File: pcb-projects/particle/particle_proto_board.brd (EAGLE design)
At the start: 33.7 x 30.5 mm, 35 parts, among them IC1 ATTINY20-MMH, IC2 DMC2400V, IC3 DMC2400V, J2 FTSH-103-XX-XXX-DH, SW1 T/S-PI SW, SW2 T/S-PI SW, SW3 T/S-PI SW

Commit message: cosmetics
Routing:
- net GND: track 142.7 -> 143.6 mm
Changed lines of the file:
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@@
 <setting verticaltext="up"/>
 </settings>
-<grid distance="12.5" unitdist="mil" unit="mil" style="lines" multiple="1" display="yes" altdistance="0.00625" altunitdist="inch" altunit="inch"/>
+<grid distance="0.635" unitdist="mm" unit="mm" style="lines" multiple="1" display="yes" altdistance="0.00625" altunitdist="inch" altunit="inch"/>
 <layers>
 <layer number="1" name="Top" color="4" fill="1" visible="yes" active="yes"/>
@@
 <wire x1="10.16" y1="14.605" x2="10.795" y2="15.24" width="0.127" layer="1"/>
 <wire x1="10.795" y1="15.24" x2="10.795" y2="16.51" width="0.127" layer="1"/>
-<wire x1="10.795" y1="16.51" x2="11.43" y2="17.145" width="0.127" layer="1"/>
-<wire x1="11.43" y1="17.145" x2="13.6525" y2="17.145" width="0.127" layer="1"/>
-<wire x1="13.6525" y1="17.145" x2="14.605" y2="16.1925" width="0.127" layer="1"/>
+<wire x1="10.795" y1="16.51" x2="11.7475" y2="17.4625" width="0.127" layer="1"/>
+<wire x1="11.7475" y1="17.4625" x2="13.335" y2="17.4625" width="0.127" layer="1"/>
+<wire x1="13.335" y1="17.4625" x2="14.605" y2="16.1925" width="0.127" layer="1"/>
 <wire x1="14.1" y1="23.845" x2="14.1" y2="25.4" width="0.127" layer="1"/>
 <wire x1="17.145" y1="21.1328" x2="17.145" y2="19.685" width="0.127" layer="1"/>
@@
 <wire x1="14.605" y1="16.1925" x2="14.605" y2="7.0375" width="0.127" layer="1"/>
 <wire x1="14.605" y1="7.0375" x2="14.88" y2="6.7625" width="0.127" layer="1"/>
-<wire x1="10.922" y1="6.35" x2="14.4675" y2="6.35" width="0.127" layer="1"/>
 <wire x1="14.4675" y1="6.35" x2="14.88" y2="6.7625" width="0.127" layer="1"/>
 <wire x1="32.385" y1="0" x2="32.385" y2="-0.635" width="0.127" layer="1"/>
@@
 <wire x1="26.3525" y1="3.175" x2="22.86" y2="6.6675" width="0.127" layer="1"/>
 <wire x1="22.86" y1="6.6675" x2="20.6375" y2="6.6675" width="0.127" layer="1"/>
+<wire x1="10.922" y1="6.35" x2="12.7" y2="6.35" width="0.127" layer="1"/>
+<wire x1="12.7" y1="6.35" x2="13.0175" y2="6.6675" width="0.127" layer="1"/>
+<wire x1="13.0175" y1="6.6675" x2="14.785" y2="6.6675" width="0.127" layer="1"/>
+<wire x1="14.785" y1="6.6675" x2="14.88" y2="6.7625" width="0.127" layer="1"/>
 <wire x1="14.605" y1="16.1925" x2="17.645" y2="14.185" width="0" layer="19" extent="1-1"/>
 </signal>
@@
 <contactref element="R1" pad="1"/>
 <contactref element="IC1" pad="13"/>
-<wire x1="8.255" y1="17.78" x2="13.6525" y2="17.78" width="0.127" layer="1"/>
+<wire x1="7.9375" y1="18.0975" x2="13.335" y2="18.0975" width="0.127" layer="1"/>
 <wire x1="15.6972" y1="19.685" x2="14.9225" y2="19.685" width="0.127" layer="1"/>
 <wire x1="14.9225" y1="19.685" x2="14.605" y2="20.0025" width="0.127" layer="1"/>
@@
 <wire x1="14.605" y1="20.6375" x2="13.97" y2="21.2725" width="0.127" layer="1"/>
 <wire x1="13.97" y1="21.2725" x2="8.255" y2="21.2725" width="0.127" layer="1"/>
-<wire x1="8.255" y1="17.78" x2="7.3025" y2="18.7325" width="0.127" layer="1"/>
+<wire x1="7.9375" y1="18.0975" x2="7.3025" y2="18.7325" width="0.127" layer="1"/>
 <wire x1="7.3025" y1="18.7325" x2="7.3025" y2="20.32" width="0.127" layer="1"/>
 <wire x1="7.3025" y1="20.32" x2="8.255" y2="21.2725" width="0.127" layer="1"/>
-<wire x1="13.6525" y1="17.78" x2="14.9225" y2="16.51" width="0.127" layer="1"/>
+<wire x1="13.335" y1="18.0975" x2="14.9225" y2="16.51" width="0.127" layer="1"/>
 <wire x1="14.9225" y1="16.51" x2="14.9225" y2="8.5725" width="0.127" layer="1"/>
 <contactref element="J2" pad="5"/>
 <contactref element="S2" pad="2"/>
 <wire x1="8.0895" y1="3.4925" x2="8.0895" y2="4.445" width="0.127" layer="1"/>
-<wire x1="8.0895" y1="4.445" x2="8.0895" y2="6.1345" width="0.127" layer="1"/>
 <wire x1="8.0895" y1="6.1345" x2="7.874" y2="6.35" width="0.127" layer="1"/>
 <wire x1="14.9225" y1="8.5725" x2="15.5575" y2="7.9375" width="0.127" layer="1"/>
@@
 <wire x1="13.1975" y1="4.445" x2="8.0895" y2="4.445" width="0.127" layer="1"/>
 <wire x1="8.5725" y1="3.4925" x2="8.0895" y2="3.4925" width="0.127" layer="1"/>
+<wire x1="8.0895" y1="4.445" x2="8.0895" y2="5.2455" width="0.127" layer="1"/>
+<wire x1="8.0895" y1="5.2455" x2="7.9375" y2="5.3975" width="0.127" layer="1"/>
+<wire x1="7.9375" y1="5.3975" x2="7.9375" y2="6.2865" width="0.127" layer="1"/>
+<wire x1="7.9375" y1="6.2865" x2="7.874" y2="6.35" width="0.127" layer="1"/>
 </signal>
 <signal name="RX_B" class="1">
@@
 <wire x1="2.54" y1="25.4" x2="5.563" y2="25.4" width="0.127" layer="1"/>
 <via x="5.3975" y="23.1775" extent="1-16" drill="0.8" shape="square"/>
-<wire x1="16.1925" y1="22.225" x2="2.54" y2="22.225" width="0.127" layer="1"/>
 <wire x1="20.955" y1="24.13" x2="6.35" y2="24.13" width="0.254" layer="16"/>
 <wire x1="6.35" y1="24.13" x2="5.3975" y2="23.1775" width="0.254" layer="16"/>
@@
 <wire x1="2.8575" y1="13.335" x2="2.54" y2="13.6525" width="0.127" layer="1"/>
 <contactref element="J2" pad="2"/>
-<wire x1="5.2455" y1="3.4925" x2="2.8575" y2="3.4925" width="0.127" layer="1"/>
-<wire x1="2.8575" y1="3.4925" x2="2.54" y2="3.81" width="0.127" layer="1"/>
-<wire x1="2.54" y1="25.4" x2="2.54" y2="0" width="1.016" layer="1"/>
+<wire x1="2.54" y1="25.4" x2="2.54" y2="23.1775" width="1.016" layer="1"/>
+<wire x1="2.54" y1="23.1775" x2="2.54" y2="3.81" width="1.016" layer="1"/>
+<wire x1="2.54" y1="3.81" x2="2.54" y2="0" width="1.016" layer="1"/>
 <wire x1="14.2875" y1="11.1125" x2="11.7475" y2="8.5725" width="0.127" layer="1"/>
 <wire x1="11.7475" y1="8.5725" x2="11.2395" y2="8.5725" width="0.127" layer="1"/>
@@
 <wire x1="17.78" y1="1.27" x2="15.875" y2="1.27" width="0.254" layer="1"/>
 <wire x1="15.875" y1="1.27" x2="14.605" y2="0" width="0.254" layer="1"/>
+<wire x1="5.3975" y1="23.1775" x2="2.54" y2="23.1775" width="0.254" layer="1"/>
+<wire x1="16.1925" y1="22.225" x2="6.35" y2="22.225" width="0.127" layer="1"/>
+<wire x1="6.35" y1="22.225" x2="5.3975" y2="23.1775" width="0.127" layer="1"/>
+<wire x1="5.2455" y1="3.4925" x2="2.8575" y2="3.4925" width="0.127" layer="1"/>
+<wire x1="2.8575" y1="3.4925" x2="2.54" y2="3.81" width="0.127" layer="1"/>
 </signal>
 <signal name="TX_B">

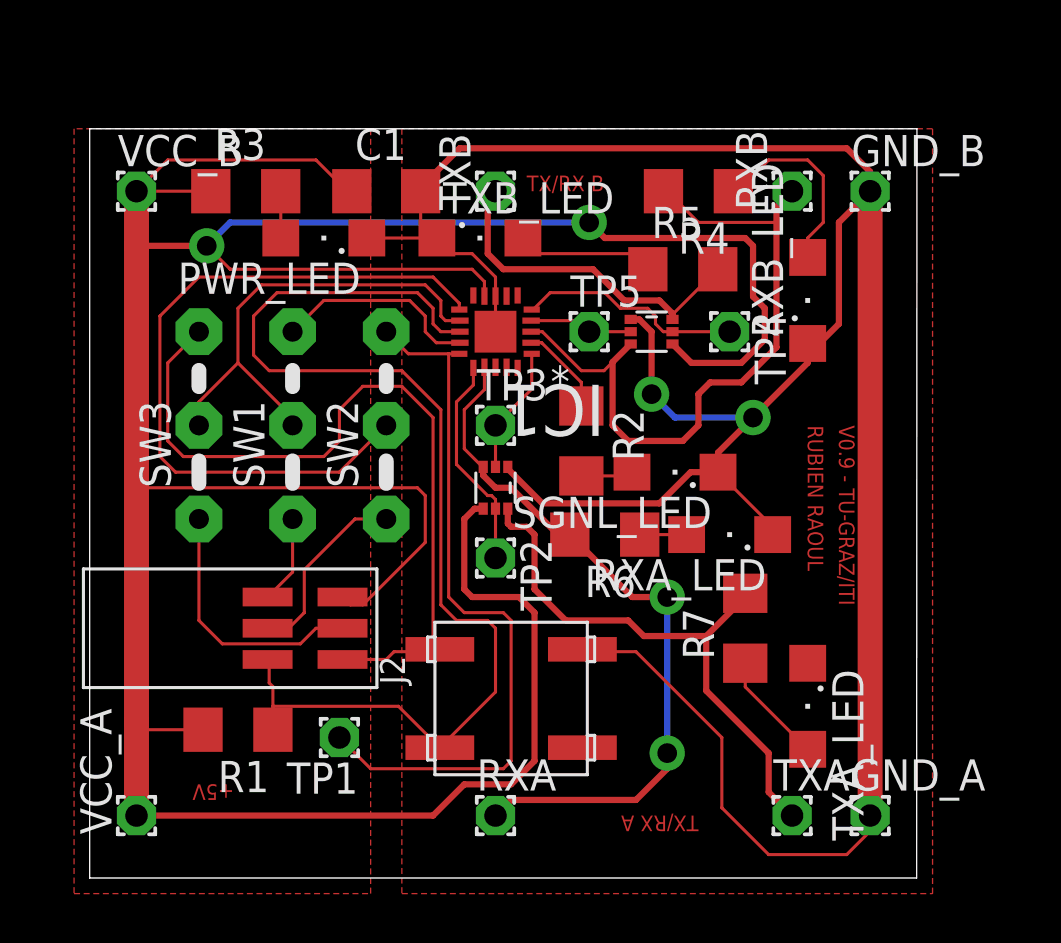
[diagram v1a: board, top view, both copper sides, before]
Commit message: changed 90° spi connector to straight one
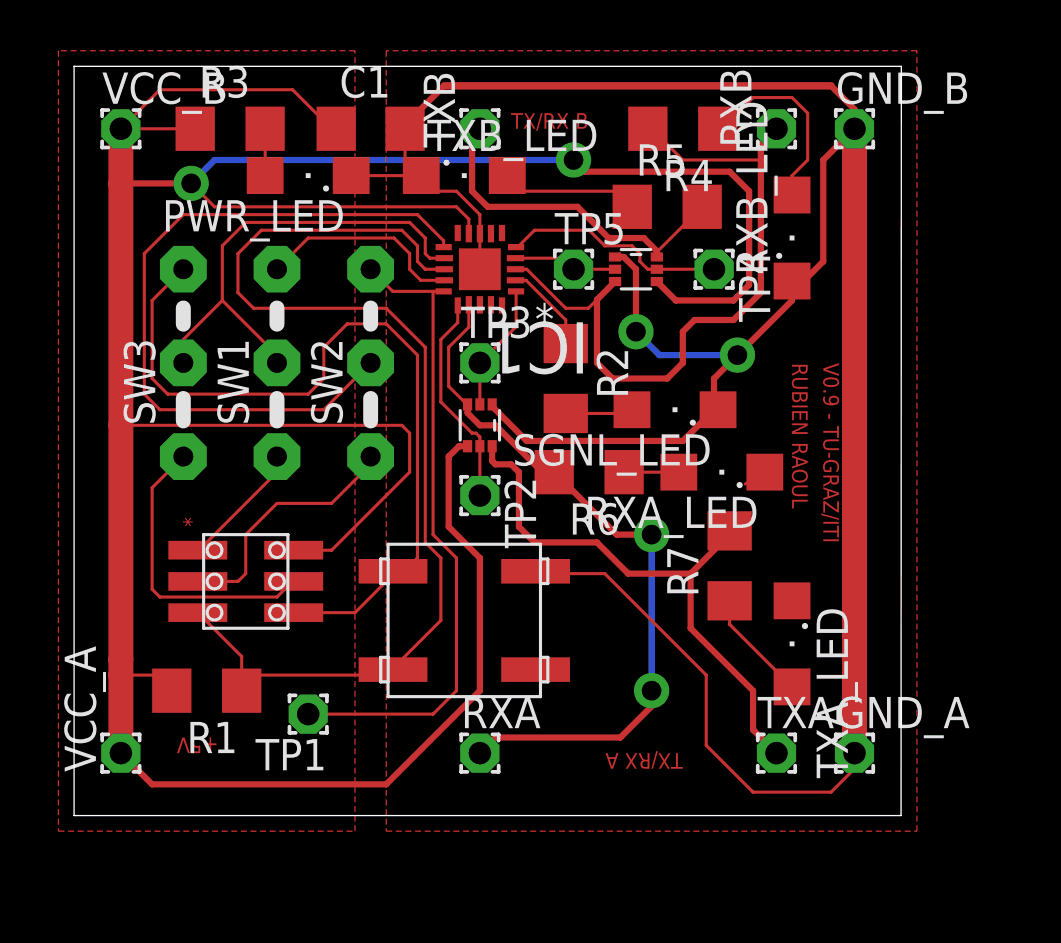
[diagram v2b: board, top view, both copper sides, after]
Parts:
- removed J2: FTSH-103-XX-XXX-DH, FTSH-103-XX-XXX-DH:FTSH-103-XX-XXX-DH
- added TPI/SPI: 20021121-00006C4LF, fci-20021121-pin-header:20021121-00006C4LF
- moved S2 3.70 mm to (15.9, 7.94)
- moved IC3 2.62 mm to (22.9, 22.2)
- moved R3 2.62 mm to (6.35, 27.9)
- moved RXB 2.62 mm to (28.6, 27.9)
- moved TP4 2.62 mm to (26.0, 22.2)
- moved C1 2.62 mm to (12.1, 27.9)
- moved GND_B 2.62 mm to (31.8, 27.9)
- moved IC1 2.62 mm to (16.5, 22.2)
- moved R4 2.62 mm to (24.8, 27.9)
- moved RXB_LED 2.62 mm to (29.2, 23.5)
- moved TP5 2.62 mm to (20.3, 22.2)
- moved TXB 2.62 mm to (16.5, 27.9)
- moved VCC_B 2.62 mm to (1.91, 27.9)
- moved R6 2.62 mm to (21.0, 14.0)
- moved SW1 2.62 mm to (8.26, 16.5)
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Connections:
- removed net N$15: J2.4, SW3.1
- removed net N$20: J2.3, SW2.1
- new net N$11: SW2.1, TPI/SPI.3
- new net N$2: SW3.1, TPI/SPI.4
- net GND: now also TPI/SPI.6; no longer J2.6
- net N$1: now also TPI/SPI.1; no longer J2.1
- net RESET: now also TPI/SPI.5; no longer J2.5
- net VCC: now also TPI/SPI.2; no longer J2.2
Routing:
- net N$2: track 0.00 -> 12.0 mm
- net N$15: track 10.6 -> 0.00 mm
- net N$11: track 0.00 -> 10.2 mm
- net N$20: track 7.31 -> 0.00 mm
- net RESET: track 47.5 -> 44.1 mm
- net SPI_SCK: track 29.5 -> 26.4 mm
- net N$1: track 3.60 -> 5.13 mm
- net VCC: track 136.6 -> 135.5 mm
- net GND: track 143.6 -> 142.6 mm
- net N$18: track 2.12 -> 2.71 mm

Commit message: small modification
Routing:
- net VCC: track 135.5 -> 119.5 mm
- net RX_A: track 29.4 -> 23.0 mm
- net GND: track 142.6 -> 138.1 mm
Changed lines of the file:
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@@
 <?xml version="1.0" encoding="utf-8"?>
 <!DOCTYPE eagle SYSTEM "eagle.dtd">
-<eagle version="7.2.0">
+<eagle version="6.5.0">
 <drawing>
 <settings>
@@
 <layer number="29" name="tStop" color="7" fill="3" visible="yes" active="yes"/>
 <layer number="30" name="bStop" color="7" fill="6" visible="no" active="yes"/>
-<layer number="31" name="tCream" color="6" fill="4" visible="yes" active="yes"/>
+<layer number="31" name="tCream" color="6" fill="4" visible="no" active="yes"/>
 <layer number="32" name="bCream" color="7" fill="5" visible="no" active="yes"/>
 <layer number="33" name="tFinish" color="6" fill="3" visible="no" active="yes"/>
@@
 <layer number="37" name="tTest" color="7" fill="1" visible="no" active="yes"/>
 <layer number="38" name="bTest" color="7" fill="1" visible="no" active="yes"/>
-<layer number="39" name="tKeepout" color="4" fill="11" visible="yes" active="yes"/>
-<layer number="40" name="bKeepout" color="1" fill="11" visible="yes" active="yes"/>
+<layer number="39" name="tKeepout" color="4" fill="11" visible="no" active="yes"/>
+<layer number="40" name="bKeepout" color="1" fill="11" visible="no" active="yes"/>
 <layer number="41" name="tRestrict" color="4" fill="10" visible="no" active="yes"/>
 <layer number="42" name="bRestrict" color="1" fill="10" visible="no" active="yes"/>
@@
 <wire x1="1.27" y1="27.94" x2="1.27" y2="2.54" width="1.016" layer="29"/>
 <wire x1="32.385" y1="27.94" x2="32.385" y2="2.54" width="1.016" layer="29"/>
+<rectangle x1="4.45020625" y1="11.69485625" x2="5.05455625" y2="12.275675" layer="29"/>
 </plain>
 <attributes>
@@
 <pass name="Default">
 <param name="RoutingGrid" value="6.25mil"/>
-<param name="AutoGrid" value="1"/>
-<param name="Efforts" value="2"/>
-<param name="TopRouterVariant" value="1"/>
 <param name="tpViaShape" value="round"/>
 <param name="PrefDir.1" value="*"/>
@@
 <contactref element="PWR_LED" pad="C"/>
 <polygon width="0.127" layer="1" isolate="0.6096">
-<vertex x="12.7" y="31.115"/>
-<vertex x="12.7" y="-0.635"/>
+<vertex x="3.40245" y="31.163734375"/>
+<vertex x="3.40245" y="-0.586265625"/>
 <vertex x="34.29" y="-0.635"/>
 <vertex x="34.29" y="31.115"/>
@@
 <wire x1="29.21" y1="21.745" x2="29.21" y2="20.955" width="0.254" layer="1"/>
 <wire x1="29.21" y1="20.955" x2="26.9875" y2="18.7325" width="0.254" layer="1"/>
-<wire x1="22.86" y1="19.685" x2="23.8125" y2="18.7325" width="0.254" layer="16"/>
-<wire x1="23.8125" y1="18.7325" x2="26.9875" y2="18.7325" width="0.254" layer="16"/>
 <wire x1="16.51" y1="23.6728" x2="16.51" y2="24.4475" width="0.127" layer="1"/>
 <wire x1="16.51" y1="24.4475" x2="15.5575" y2="25.4" width="0.127" layer="1"/>
@@
 <wire x1="13.0175" y1="9.8425" x2="11.43" y2="8.255" width="0.127" layer="1"/>
 <wire x1="13.335" y1="9.8425" x2="13.97" y2="10.4775" width="0.127" layer="1"/>
-<wire x1="8.89" y1="8.255" x2="8.935" y2="8.255" width="0" layer="19" extent="1-1"/>
-<wire x1="17.01" y1="16.725" x2="13.97" y2="18.7325" width="0" layer="19" extent="1-1"/>
+<wire x1="26.035" y1="17.78" x2="22.86" y2="19.685" width="0" layer="19" extent="1-1"/>
+<wire x1="13.97" y1="18.7325" x2="17.01" y2="16.725" width="0" layer="19" extent="1-1"/>
 </signal>
 <signal name="PWR/TX_B">
@@
 <contactref element="R3" pad="1"/>
 <polygon width="0.127" layer="1" isolate="0.6096">
-<vertex x="11.43" y="31.115"/>
+<vertex x="2.619234375" y="31.01753125"/>
 <vertex x="-0.635" y="31.115"/>
 <vertex x="-0.635" y="-0.635"/>
-<vertex x="11.43" y="-0.635"/>
+<vertex x="2.619234375" y="-0.73246875"/>
 </polygon>
 <wire x1="23.71" y1="21.725" x2="24.48" y2="20.955" width="0.254" layer="1"/>
@@
 <wire x1="1.905" y1="27.94" x2="4.928" y2="27.94" width="0.127" layer="1"/>
 <via x="4.7625" y="25.7175" extent="1-16" drill="0.8" shape="square"/>
-<wire x1="20.32" y1="26.67" x2="5.715" y2="26.67" width="0.254" layer="16"/>
-<wire x1="5.715" y1="26.67" x2="4.7625" y2="25.7175" width="0.254" layer="16"/>
 <wire x1="10.665" y1="27.94" x2="10.4775" y2="27.94" width="0.127" layer="1"/>
 <wire x1="10.4775" y1="27.94" x2="8.89" y2="29.5275" width="0.127" layer="1"/>
@@
 <wire x1="1.905" y1="2.54" x2="3.175" y2="1.27" width="0.254" layer="1"/>
 <wire x1="3.175" y1="1.27" x2="12.7" y2="1.27" width="0.254" layer="1"/>
+<wire x1="16.06" y1="24.2625" x2="20.32" y2="26.67" width="0" layer="19" extent="1-1"/>
+<wire x1="3.9755" y1="5.08" x2="4.1275" y2="5.715" width="0" layer="19" extent="1-1"/>
 </signal>
 <signal name="TX_B">
@@
 <wire x1="19.533" y1="13.97" x2="22.073" y2="11.43" width="0.254" layer="1"/>
 <wire x1="22.073" y1="11.43" x2="23.495" y2="11.43" width="0.254" layer="1"/>
-<wire x1="23.495" y1="11.43" x2="23.495" y2="5.08" width="0.254" layer="16"/>
 <wire x1="22.225" y1="3.175" x2="23.495" y2="4.445" width="0.254" layer="1"/>
 <wire x1="23.495" y1="4.445" x2="23.495" y2="5.08" width="0.254" layer="1"/>
+<wire x1="23.495" y1="5.08" x2="23.495" y2="11.43" width="0" layer="19" extent="1-1"/>
 </signal>
 <signal name="SPI_MISO">
